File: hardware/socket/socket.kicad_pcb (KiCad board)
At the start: 4 copper layers, 80 x 34.5 mm, 80 parts, among them J101 Cortex, J102 DX07S016JA3, J201 NE8FAH, J301 SJ2-25404B-SMT-TR, J401 SJ2-25404B-SMT-TR, SW101 SKSG, SW102 SKSG, SW103 SKSG, SW104 SKSG, SW105 SKSG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

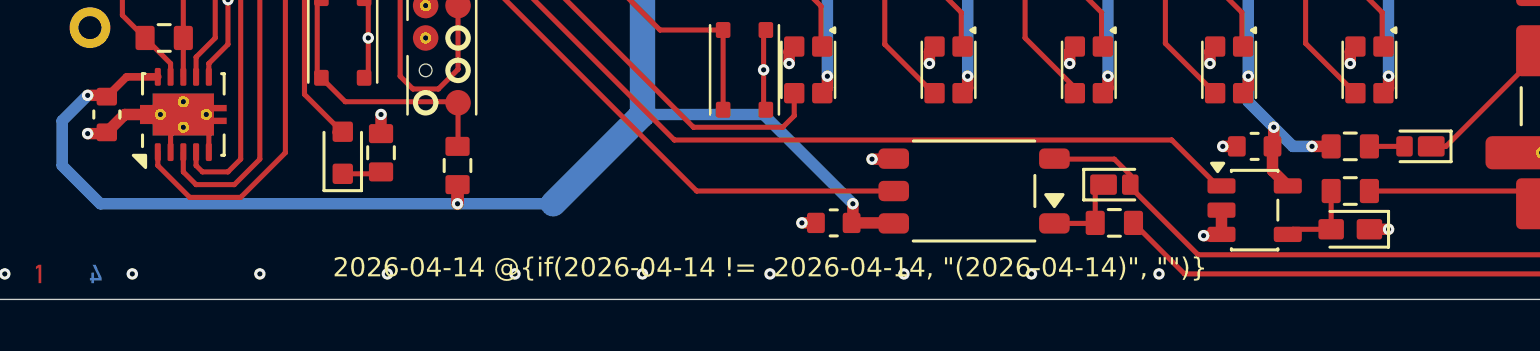
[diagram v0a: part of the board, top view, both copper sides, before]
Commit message: Split into socket and plug
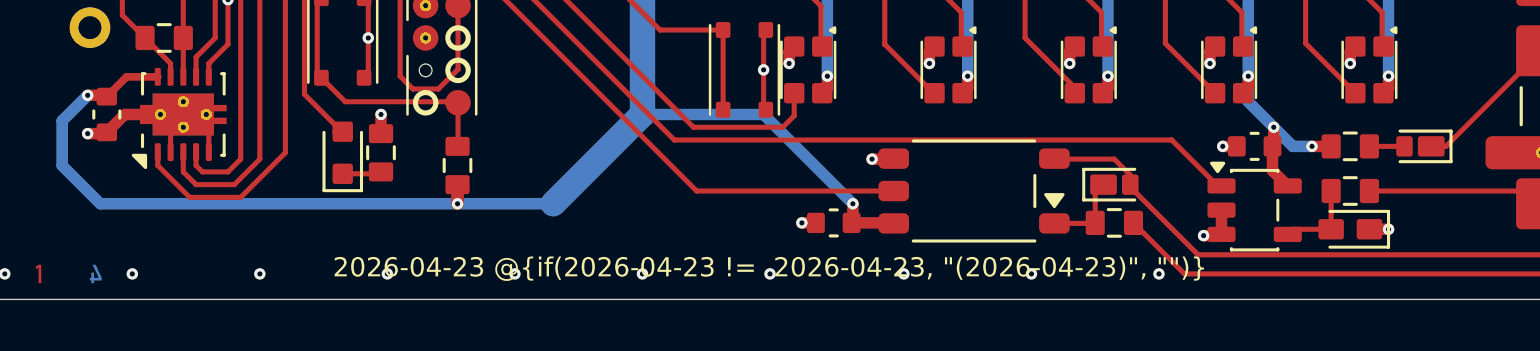
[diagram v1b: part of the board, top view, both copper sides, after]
